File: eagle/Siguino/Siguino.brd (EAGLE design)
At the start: 71 x 39 mm, 48 parts, among them J1 FTDI, J4 10118193-0001LF, Q1 MOSFET P-CH 20V 5.3A SOT-23, Q2 MOSFET P-CH 20V 5.3A SOT-23, U1 ATMEGA328P_TQFP, U2 LIS3MDLTR_LIS3MDLTR, U3 SPARKFUN-SENSORS_LIS3DH, U4 BME280, U5 FT232RL, U6 MAX1724EZK33+T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

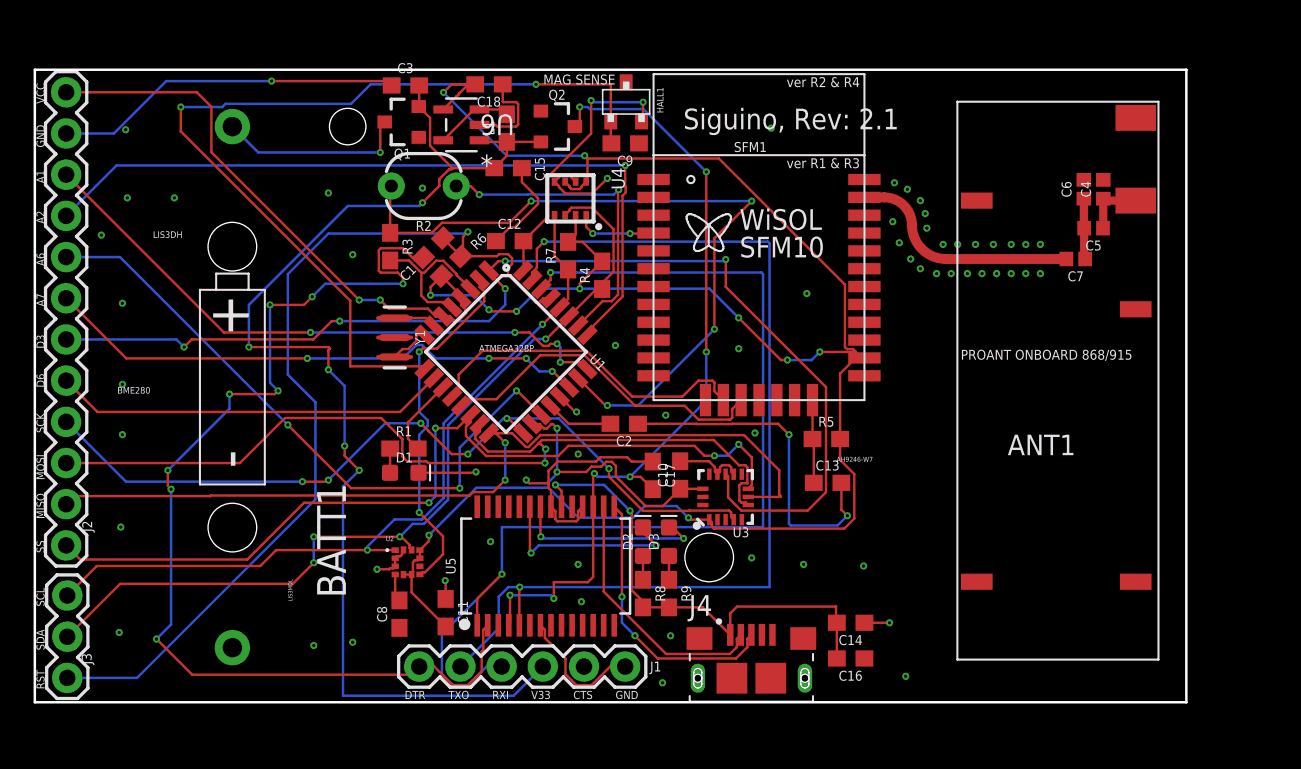
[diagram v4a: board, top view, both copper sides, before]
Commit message: Moved components and resized board to fit box
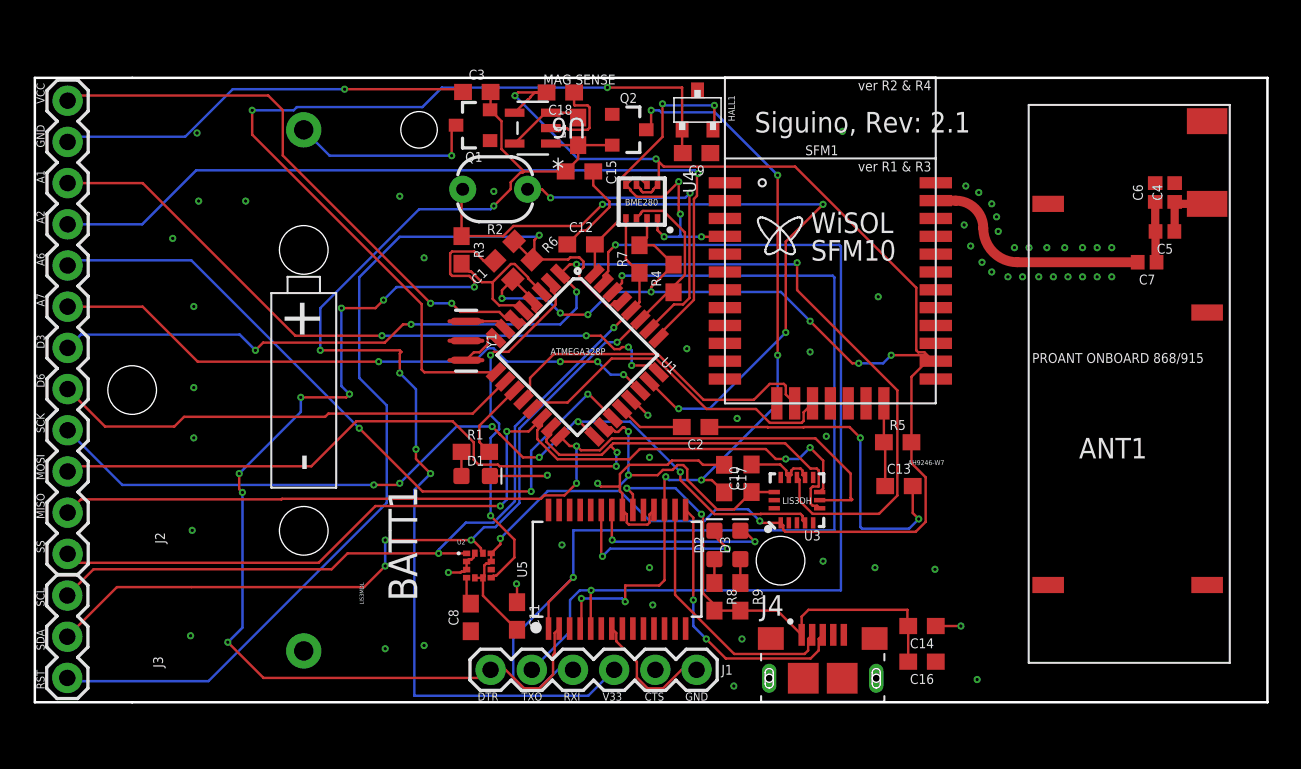
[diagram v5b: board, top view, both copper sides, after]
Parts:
- moved C9 4.44 mm to (40.8, 33.9)
- moved C18 4.43 mm to (32.4, 37.6)
- moved HALL1 4.43 mm to (40.9, 36.5)
- moved C3 4.42 mm to (27.2, 37.6)
- moved C14 4.40 mm to (54.7, 4.70)
- moved C16 4.40 mm to (54.7, 2.50)
- moved C4 4.40 mm to (70.3, 31.4)
- moved C5 4.40 mm to (69.7, 29.0)
- moved R4 4.40 mm to (39.4, 26.1)
- moved R5 4.40 mm to (53.2, 16.0)
- moved C11 4.40 mm to (29.7, 5.32)
- moved J1 4.40 mm to (28.1, 2.00)
- moved U1 4.40 mm to (33.5, 21.4)
- moved ANT1 4.40 mm to (67.3, 21.0)
- moved BATT1 4.40 mm to (16.6, 19.2)
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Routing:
- net GND: track 112.2 -> 119.6 mm, vias 66 -> 67
- net INT1: track 71.0 -> 75.9 mm
- net D6: track 24.3 -> 29.1 mm
- net RESET: track 57.8 -> 62.2 mm
- net A6: track 39.8 -> 44.2 mm
- net MOSI: track 56.2 -> 60.6 mm
- net SDA: track 54.4 -> 58.7 mm
- net SCL: track 48.5 -> 52.8 mm
- net A2: track 47.2 -> 51.5 mm
- net VCC: track 181.4 -> 185.6 mm
- net SS: track 54.2 -> 58.3 mm
- net A7: track 34.0 -> 38.1 mm
- net A1: track 37.8 -> 41.9 mm
- net SCK: track 50.4 -> 54.5 mm
- net MISO: track 53.9 -> 57.6 mm
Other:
- board size 71 x 39 mm -> 76 x 38.5 mm

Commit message: ufl
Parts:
- added J5: U.FL, SparkFun-Connectors:U.FL
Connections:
- removed net CTS: J1.5
- removed net N$6: C7.2, SFM1.30
- new net WISOL_ANT: C7.2, J5.FEED, SFM1.30
- net GND: now also J1.5, J5.1, J5.2
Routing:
- net WISOL_ANT: track 0.00 -> 14.0 mm
- net N$6: track 14.0 -> 0.00 mm
- net LIGHT_SENSE: track 45.9 -> 42.7 mm
- net VCC: track 185.6 -> 188.1 mm
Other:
- outline, holes or cut-outs redrawn
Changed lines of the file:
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@@
 <plain>
 <text x="44.38" y="35.13" size="1.27" layer="21">Siguino, Rev: 2.1</text>
-<wire x1="0" y1="0" x2="6" y2="0" width="0.1524" layer="20"/>
-<wire x1="6" y1="0" x2="76" y2="0" width="0.1524" layer="20"/>
+<wire x1="0" y1="0" x2="76" y2="0" width="0.1524" layer="20"/>
 <wire x1="76" y1="0" x2="76" y2="38.5" width="0.1524" layer="20"/>
-<wire x1="76" y1="38.5" x2="6" y2="38.5" width="0.1524" layer="20"/>
-<wire x1="6" y1="38.5" x2="0" y2="38.5" width="0.1524" layer="20"/>
+<wire x1="76" y1="38.5" x2="0" y2="38.5" width="0.1524" layer="20"/>
 <wire x1="0" y1="38.5" x2="0" y2="0" width="0.1524" layer="20"/>
-<hole x="45.98" y="8.73" drill="3"/>
+<hole x="51.78" y="8.13" drill="3"/>
 <text x="37.6" y="0.1" size="0.5" layer="21">CTS</text>
 <text x="40.1" y="0.1" size="0.5" layer="21">GND</text>
@@
 <attribute name="PROD_ID" value="SI2323DDS-T1-GE3" x="36.6" y="35.3" size="1.778" layer="27" rot="R270" display="off"/>
 </element>
+<element name="J5" library="SparkFun-Connectors" package="U.FL" value="U.FL" x="52" y="30.9" smashed="yes">
+<attribute name="NAME" x="50.73" y="33.44" size="0.6096" layer="25" font="vector" ratio="20"/>
+<attribute name="PROD_ID" value="CONN-09193" x="52" y="30.9" size="1.778" layer="27" display="off"/>
+<attribute name="SF_ID" value="WRL-09144" x="52" y="30.9" size="1.778" layer="27" display="off"/>
+<attribute name="VALUE" x="50.73" y="28.36" size="0.6096" layer="27" font="vector" ratio="20" align="top-left"/>
+</element>
 </elements>
 <signals>
@@
 <via x="34.7" y="13.5" extent="1-16" drill="0.2"/>
 <via x="47.8" y="21.6" extent="1-16" drill="0.2"/>
-<via x="51.8" y="8.3" extent="1-16" drill="0.2"/>
+<via x="46.1" y="8.4" extent="1-16" drill="0.2"/>
 <via x="55.5" y="8.2" extent="1-16" drill="0.2"/>
 <via x="21.6" y="3.3" extent="1-16" drill="0.2"/>
@@
 <wire x1="36.76816875" y1="18.647515625" x2="36.852484375" y2="18.647515625" width="0.1524" layer="1"/>
 <wire x1="36.852484375" y1="18.647515625" x2="37.8" y2="17.7" width="0.1524" layer="1"/>
+<contactref element="J5" pad="2"/>
+<contactref element="J5" pad="1"/>
+<contactref element="J1" pad="5"/>
 </signal>
 <signal name="VCC">
@@
 <wire x1="54.8512" y1="21.5788" x2="55.4" y2="21.03" width="0.1524" layer="1"/>
 <wire x1="54.3488" y1="25.55394375" x2="54.3488" y2="21.6966625" width="0.1524" layer="1"/>
-<wire x1="46.87654375" y1="33.0262" x2="54.3488" y2="25.55394375" width="0.1524" layer="1"/>
 <wire x1="39.38" y1="26.98" x2="38" y2="25.6" width="0.1524" layer="1"/>
 <wire x1="38" y1="25.6" x2="38" y2="25.3" width="0.1524" layer="1"/>
@@
 <wire x1="36.599996875" y1="16.695" x2="36.6" y2="16.695" width="0.1524" layer="1"/>
 <wire x1="54.05" y1="14.7445375" x2="54.05" y2="16.03" width="0.1524" layer="1"/>
+<wire x1="46.87654375" y1="33.0262" x2="48.8" y2="31.10274375" width="0.1524" layer="1"/>
+<wire x1="48.8" y1="31.10274375" x2="48.8" y2="26.8" width="0.1524" layer="1"/>
+<wire x1="48.8" y1="26.8" x2="50.04605625" y2="25.55394375" width="0.1524" layer="1"/>
+<wire x1="50.04605625" y1="25.55394375" x2="54.3488" y2="25.55394375" width="0.1524" layer="1"/>
 </signal>
 <signal name="N$2">
@@
 <wire x1="28.87835625" y1="28.74" x2="29.503053125" y2="29.364696875" width="0.1524" layer="1"/>
 <wire x1="29.503053125" y1="29.364696875" x2="33.664696875" y2="29.364696875" width="0.1524" layer="1"/>
-<wire x1="35" y1="30.7" x2="48.6" y2="30.7" width="0.1524" layer="16"/>
-<via x="48.6" y="30.7" extent="1-16" drill="0.2"/>
-<wire x1="48.6" y1="30.7" x2="46.3" y2="28.4" width="0.1524" layer="1"/>
-<wire x1="46.3" y1="28.4" x2="46.3" y2="22.8" width="0.1524" layer="1"/>
+<wire x1="35" y1="30.7" x2="46.3" y2="30.7" width="0.1524" layer="16"/>
+<via x="46.3" y="30.7" extent="1-16" drill="0.2"/>
+<wire x1="46.3" y1="30.7" x2="46.3" y2="22.8" width="0.1524" layer="1"/>
 <via x="46.3" y="22.8" extent="1-16" drill="0.2"/>
 <wire x1="46.3" y1="22.8" x2="41.6" y2="18.1" width="0.1524" layer="16"/>
@@
 <wire x1="24.017190625" y1="20.344571875" x2="23.8497625" y2="20.512" width="0.1524" layer="1"/>
 </signal>
-<signal name="N$6">
+<signal name="WISOL_ANT">
 <contactref element="SFM1" pad="30"/>
 <contactref element="C7" pad="2"/>
@@
 <wire x1="60.58" y1="27.13" x2="68" y2="27.13" width="0.6096" layer="1"/>
 <wire x1="55.55" y1="30.93" x2="56.78" y2="30.93" width="0.6096" layer="1"/>
+<contactref element="J5" pad="FEED"/>
+<wire x1="53.525" y1="30.9" x2="55.55" y2="30.93" width="0" layer="19" extent="1-1"/>
 </signal>
 <signal name="5V">
@@
 <wire x1="42.6" y1="2.7" x2="47.8345375" y2="2.7" width="0.1524" layer="1"/>
 </signal>
-<signal name="CTS">
-<contactref element="J1" pad="5"/>
-</signal>
 <signal name="N$17">

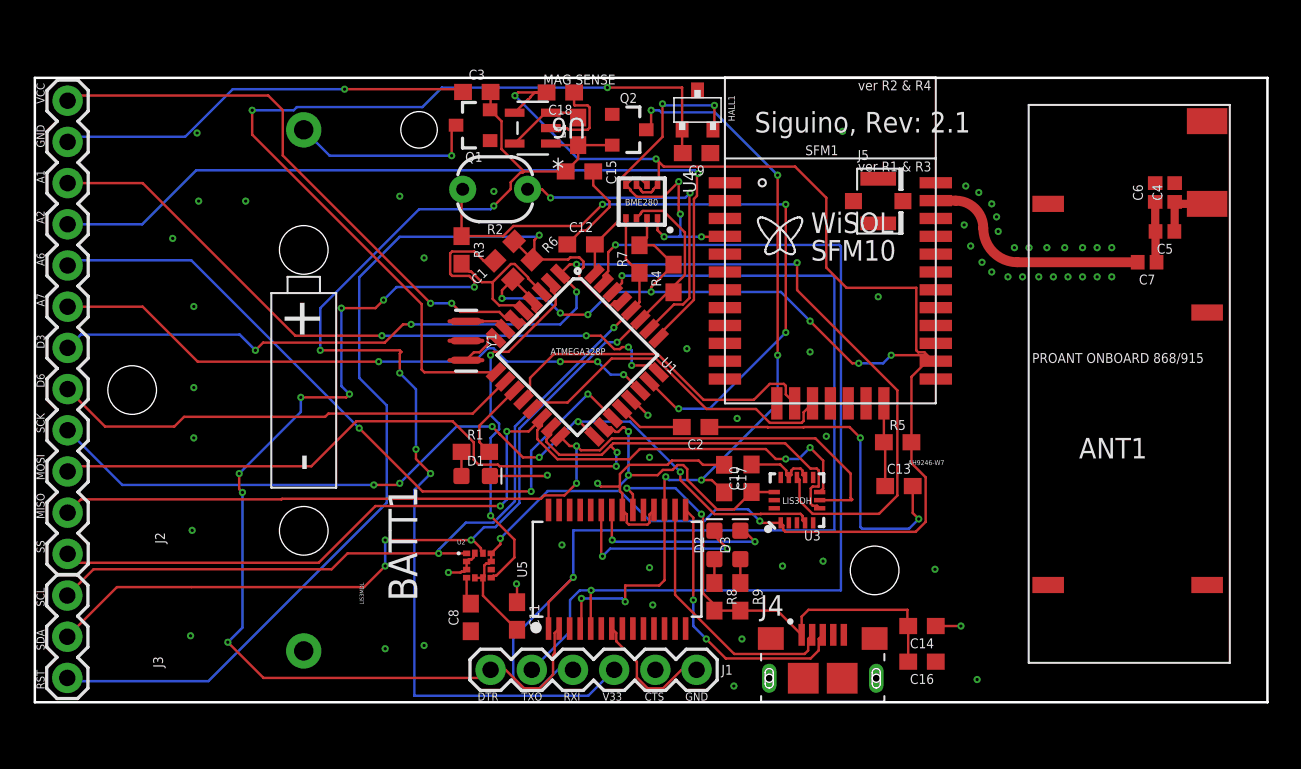
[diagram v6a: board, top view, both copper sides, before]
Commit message: Added PPTC over current protection
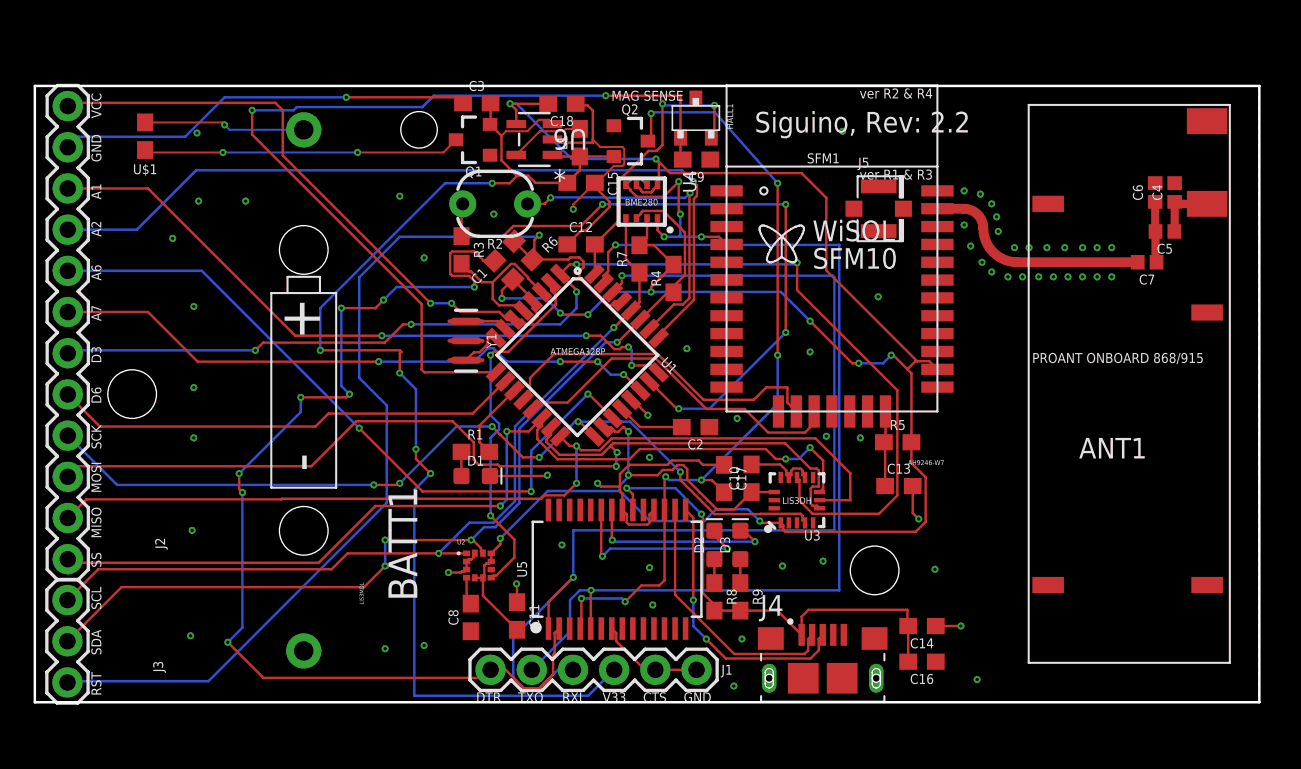
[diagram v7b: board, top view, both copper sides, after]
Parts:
- added U$1: PPTC, Siguino:0603
- moved Q1 0.90 mm to (27.1, 34.7)
- moved R2 0.90 mm to (28.4, 30.7)
- moved C18 0.71 mm to (32.5, 36.9)
- moved L1 0.71 mm to (33.6, 34.5)
- moved C15 0.71 mm to (33.7, 32.0)
- moved Q2 0.71 mm to (36.7, 34.6)
- moved U6 0.71 mm to (30.8, 34.7)
- moved C3 0.70 mm to (27.2, 36.9)
- moved HALL1 0.51 mm to (40.8, 36.0)
- moved SFM1 0.51 mm to (49.1, 25.5)
- moved J5 0.47 mm to (52.0, 30.4)
- moved C9 0.40 mm to (40.8, 33.5)
- moved J2 0.33 mm to (2.03, 8.82)
- moved J3 0.28 mm to (2.01, 1.22)
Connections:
- new net VSAFE: Q1.3, U$1.2
- net N$17: no longer U6.3
- net VBAT: now also U$1.1; no longer Q1.3
- net VBAT2: now also U6.3
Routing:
- net VSAFE: track 0.00 -> 19.6 mm, vias 0 -> 2
- net GND: track 119.6 -> 106.5 mm, vias 67 -> 68
- net VCC: track 188.1 -> 183.7 mm
- net VBAT2: track 73.5 -> 76.6 mm
- net VBAT: track 11.8 -> 9.97 mm
- net LIGHT_SENSE: track 42.7 -> 41.8 mm
- net HALL_SENSE: track 17.0 -> 17.8 mm
- net INT1: track 75.9 -> 75.2 mm
- net SIG_RX: track 21.0 -> 21.5 mm
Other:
- board size 76 x 38.5 mm -> 75.5 x 38 mm
- board text added: "Siguino, Rev: 2.2"
- board text removed: "Siguino, Rev: 2.1"
